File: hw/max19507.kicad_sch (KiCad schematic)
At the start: 33 parts, among them U9 MAX19517

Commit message: WIP: intermediate commit (routing)
will try to update library footprints
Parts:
- removed R57, R59: 232DNL, Resistor_SMD:R_0603_1608Metric, symbol Device:R_Small
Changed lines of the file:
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@@
-	)
-	(junction
-		(at 186.69 76.2)
-		(diameter 0)
-		(color 0 0 0 0)
 	)
 	(junction
@@
 	)
 	(junction
-		(at 186.69 96.52)
-		(diameter 0)
-		(color 0 0 0 0)
-	)
-	(junction
 		(at 165.1 68.58)
 		(diameter 0)
@@
 	)
 	(junction
-		(at 186.69 91.44)
-		(diameter 0)
-		(color 0 0 0 0)
-	)
-	(junction
 		(at 137.16 96.52)
 		(diameter 0)
@@
 	(junction
 		(at 171.45 76.2)
-		(diameter 0)
-		(color 0 0 0 0)
-	)
-	(junction
-		(at 186.69 81.28)
 		(diameter 0)
 		(color 0 0 0 0)
@@
 	(wire
 		(pts
-			(xy 171.45 76.2) (xy 186.69 76.2)
+			(xy 171.45 76.2) (xy 196.85 76.2)
 		)
 		(stroke
@@
 	(wire
 		(pts
-			(xy 186.69 96.52) (xy 196.85 96.52)
+			(xy 171.45 96.52) (xy 196.85 96.52)
 		)
 		(stroke
@@
 	(wire
 		(pts
-			(xy 171.45 91.44) (xy 186.69 91.44)
+			(xy 171.45 91.44) (xy 196.85 91.44)
 		)
 		(stroke
@@
 	(wire
 		(pts
-			(xy 171.45 81.28) (xy 186.69 81.28)
+			(xy 171.45 81.28) (xy 196.85 81.28)
 		)
 		(stroke
@@
 	(wire
 		(pts
-			(xy 171.45 96.52) (xy 186.69 96.52)
-		)
-		(stroke
-			(width 0)
-			(type default)
-		)
-	)
-	(wire
-		(pts
 			(xy 201.93 82.55) (xy 193.04 82.55)
 		)
@@
 	(wire
 		(pts
-			(xy 186.69 76.2) (xy 196.85 76.2)
-		)
-		(stroke
-			(width 0)
-			(type default)
-		)
-	)
-	(wire
-		(pts
 			(xy 226.06 63.5) (xy 226.06 50.8)
 		)
@@
 	(wire
 		(pts
-			(xy 186.69 91.44) (xy 196.85 91.44)
-		)
-		(stroke
-			(width 0)
-			(type default)
-		)
-	)
-	(wire
-		(pts
 			(xy 196.85 81.28) (xy 196.85 80.01)
 		)
@@
 		(pts
 			(xy 148.59 91.44) (xy 171.45 91.44)
-		)
-		(stroke
-			(width 0)
-			(type default)
-		)
-	)
-	(wire
-		(pts
-			(xy 186.69 81.28) (xy 196.85 81.28)
 		)
 		(stroke
@@
 					(unit 1)
 				)
-			)
-		)
-	)
-	(symbol
-		(lib_id "Device:R_Small")
-		(at 186.69 78.74 180)
-		(unit 1)
-		(exclude_from_sim no)
-		(in_bom no)
-		(on_board yes)
-		(dnp yes)
-		(property "Reference" "R57"
-			(at 189.23 78.74 90)
-			(effects
-				(font
-					(size 1.27 1.27)
-				)
-			)
-		)
-		(property "Value" "232DNL"
-			(at 191.77 78.74 90)
-			(effects
-				(font
-					(size 1.27 1.27)
-				)
-			)
-		)
-		(property "Footprint" "Resistor_SMD:R_0603_1608Metric"
-			(at 186.69 78.74 0)
-			(effects
-				(font
-					(size 1.27 1.27)
-				)
-				(hide yes)
-			)
-		)
-		(property "Datasheet" "~"
-			(at 186.69 78.74 0)
-			(effects
-				(font
-					(size 1.27 1.27)
-				)
-				(hide yes)
-			)
-		)
-		(property "Description" ""
-			(at 186.69 78.74 0)
-			(effects
-				(font
-					(size 1.27 1.27)
-				)
-				(hide yes)
-			)
-		)
-		(pin "1"
-		)
-		(pin "2"
-		)
-		(instances
-			(project "usbadc"
-				(path "/7c8a1f8d-8834-4c9b-aaae-1f231e9b09a1/00000000-0000-0000-0000-0000612b1274"
-					(reference "R57")
-					(unit 1)
-				)
-			)
-		)
-	)
-	(symbol
-		(lib_id "Device:R_Small")
-		(at 186.69 93.98 180)
-		(unit 1)
-		(exclude_from_sim no)
-		(in_bom no)
-		(on_board yes)
-		(dnp yes)
-		(property "Reference" "R59"
-			(at 189.23 93.98 90)
-			(effects
-				(font
-					(size 1.27 1.27)
-				)
-			)
-		)
-		(property "Value" "232DNL"
-			(at 191.77 93.98 90)
-			(effects
-				(font
-					(size 1.27 1.27)
-				)
-			)
-		)
-		(property "Footprint" "Resistor_SMD:R_0603_1608Metric"
-			(at 186.69 93.98 0)
-			(effects
-				(font
-					(size 1.27 1.27)
-				)
-				(hide yes)
-			)
-		)
-		(property "Datasheet" "~"
-			(at 186.69 93.98 0)
-			(effects
-				(font
-					(size 1.27 1.27)
-				)
-				(hide yes)
-			)
-		)
-		(property "Description" ""
-			(at 186.69 93.98 0)
-			(effects
-				(font
-					(size 1.27 1.27)
-				)
-				(hide yes)
-			)
-		)
-		(pin "1"
-		)
-		(pin "2"
-		)
-		(instances
-			(project "usbadc"
-				(path "/7c8a1f8d-8834-4c9b-aaae-1f231e9b09a1/00000000-0000-0000-0000-0000612b1274"
-					(reference "R59")
-					(unit 1)
-				)

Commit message: updated parts assignments
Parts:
- C29, C30, C34, C35: Manufacturer (none) -> Kemet; Part (none) -> C0603C103J5RACTU
- C49, C58, C59, C60: Manufacturer (none) -> TDK; Part (none) -> C1005X7R1E104K050BB
- R36, R37, R77, R78: Manufacturer (none) -> Stackpole; Part (none) -> RMCF0603FT301R
- R38, R39, R40, R41: Manufacturer (none) -> Stackpole; Part (none) -> RMCF0603FT75R0
- R43, R44, R45, R46: Manufacturer (none) -> Stackpole; Part (none) -> RMCF0603FT226R
- U9: Manufacturer (none) -> AD; Part (none) -> MAX19517ETM+

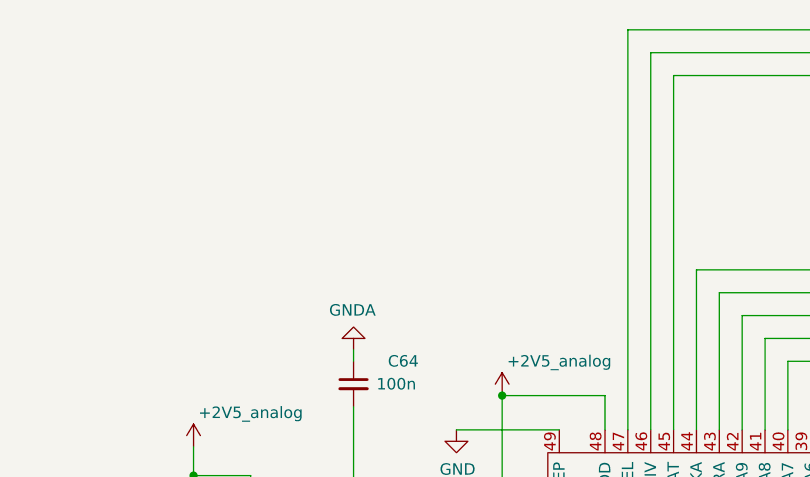
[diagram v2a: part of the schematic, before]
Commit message: connected versaclock CLKSEL to ULPI RSTB (share FPGA pin)
ULPI Rstb is unlikely to be used

Also: - update of kicad to 9.0 (many library footprints updated)
      - added sheet titles, author
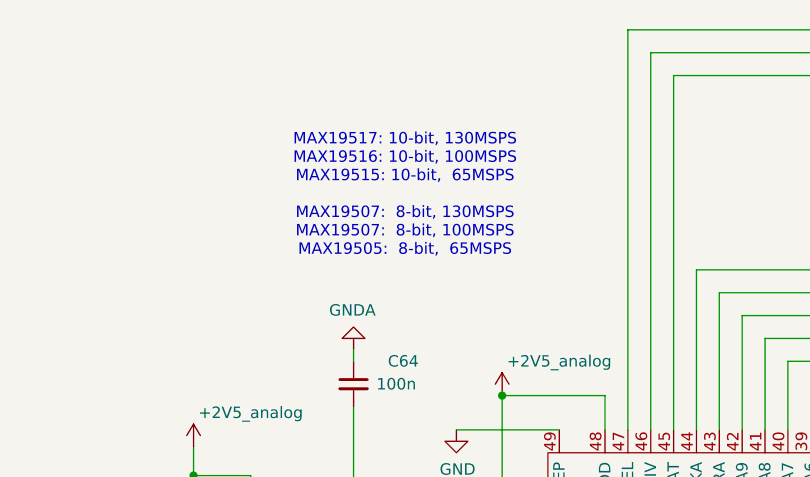
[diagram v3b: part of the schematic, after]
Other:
- note added: "MAX19517: 10-bit, 130MSPS MAX19516: 10-bit, 100MSPS MAX19515: 10-bit, 65MSPS MAX19507: 8-bit, 130MSPS MAX19507: 8-bit, 100MSPS MAX19505: 8-bit, 65MSPS"
- company: (none) -> Till Straumann
- title: (none) -> Dual-Channel ADC
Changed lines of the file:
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@@
 (kicad_sch
-	(version 20231120)
+	(version 20250114)
 	(generator "eeschema")
-	(generator_version "8.0")
+	(generator_version "9.0")
 	(paper "A4")
+	(title_block
+		(title "Dual-Channel ADC")
+		(rev "3.3b")
+		(company "Till Straumann")
+	)
+	(text "MAX19517: 10-bit, 130MSPS\nMAX19516: 10-bit, 100MSPS\nMAX19515: 10-bit,  65MSPS\n\nMAX19507:  8-bit, 130MSPS\nMAX19507:  8-bit, 100MSPS\nMAX19505:  8-bit,  65MSPS"
+		(exclude_from_sim no)
+		(at 188.595 37.465 0)
+		(effects
+			(font
+				(size 1.27 1.27)
+			)
+		)
+	)
 	(junction
 		(at 130.81 86.36)

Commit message: Added licensing information
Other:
- company: Till Straumann -> Copyright Till Straumann, 2025
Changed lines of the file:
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@@
 		(title "Dual-Channel ADC")
 		(rev "3.3b")
-		(company "Till Straumann")
+		(company "Copyright Till Straumann, 2025")
+		(comment 1 "License: CERN-OHL-P v2")
 	)
 	(text "MAX19517: 10-bit, 130MSPS\nMAX19516: 10-bit, 100MSPS\nMAX19515: 10-bit,  65MSPS\n\nMAX19507:  8-bit, 130MSPS\nMAX19507:  8-bit, 100MSPS\nMAX19505:  8-bit,  65MSPS"
